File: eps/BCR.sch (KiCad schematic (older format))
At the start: 3 parts, among them U23 LT3652EMSE, U25 LT3652EMSE, U26 LT3652EMSE

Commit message: bcr
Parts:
- added J?: SA1A, symbol Connector:Conn_01x05_Male
- added J?: SA1B, symbol Connector:Conn_01x05_Male
- added J?: SA2A, symbol Connector:Conn_01x05_Male
- added J?: SA2B, symbol Connector:Conn_01x05_Male
- added J?: SA3A, symbol Connector:Conn_01x05_Male
- added J?: SA3B, symbol Connector:Conn_01x05_Male
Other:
- moved on the sheet: U23, U25, U26
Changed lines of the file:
@@
 L Battery_Management:LT3652EMSE U23
 U 1 1 61832F84
-P 5100 2850
-F 0 "U23" H 5100 3531 50  0000 C CNN
-F 1 "LT3652EMSE" H 5100 3440 50  0000 C CNN
-F 2 "Package_SO:MSOP-12-1EP_3x4mm_P0.65mm_EP1.65x2.85mm" H 5100 2250 50  0001 C CNN
-F 3 "https://www.analog.com/media/en/technical-documentation/data-sheets/3652fe.pdf" H 5700 2050 50  0001 C CNN
-	1    5100 2850
+P 4100 2100
+F 0 "U23" H 4100 2781 50  0000 C CNN
+F 1 "LT3652EMSE" H 4100 2690 50  0000 C CNN
+F 2 "Package_SO:MSOP-12-1EP_3x4mm_P0.65mm_EP1.65x2.85mm" H 4100 1500 50  0001 C CNN
+F 3 "https://www.analog.com/media/en/technical-documentation/data-sheets/3652fe.pdf" H 4700 1300 50  0001 C CNN
+	1    4100 2100
 	1    0    0    -1
 $EndComp
@@
 L Battery_Management:LT3652EMSE U25
 U 1 1 6183C8D2
-P 7150 2850
-F 0 "U25" H 7150 3531 50  0000 C CNN
-F 1 "LT3652EMSE" H 7150 3440 50  0000 C CNN
-F 2 "Package_SO:MSOP-12-1EP_3x4mm_P0.65mm_EP1.65x2.85mm" H 7150 2250 50  0001 C CNN
-F 3 "https://www.analog.com/media/en/technical-documentation/data-sheets/3652fe.pdf" H 7750 2050 50  0001 C CNN
-	1    7150 2850
+P 4150 4350
+F 0 "U25" H 4150 5031 50  0000 C CNN
+F 1 "LT3652EMSE" H 4150 4940 50  0000 C CNN
+F 2 "Package_SO:MSOP-12-1EP_3x4mm_P0.65mm_EP1.65x2.85mm" H 4150 3750 50  0001 C CNN
+F 3 "https://www.analog.com/media/en/technical-documentation/data-sheets/3652fe.pdf" H 4750 3550 50  0001 C CNN
+	1    4150 4350
 	1    0    0    -1
 $EndComp
@@
 L Battery_Management:LT3652EMSE U26
 U 1 1 6183D07C
-P 8800 2850
-F 0 "U26" H 8800 3531 50  0000 C CNN
-F 1 "LT3652EMSE" H 8800 3440 50  0000 C CNN
-F 2 "Package_SO:MSOP-12-1EP_3x4mm_P0.65mm_EP1.65x2.85mm" H 8800 2250 50  0001 C CNN
-F 3 "https://www.analog.com/media/en/technical-documentation/data-sheets/3652fe.pdf" H 9400 2050 50  0001 C CNN
-	1    8800 2850
+P 4200 6250
+F 0 "U26" H 4200 6931 50  0000 C CNN
+F 1 "LT3652EMSE" H 4200 6840 50  0000 C CNN
+F 2 "Package_SO:MSOP-12-1EP_3x4mm_P0.65mm_EP1.65x2.85mm" H 4200 5650 50  0001 C CNN
+F 3 "https://www.analog.com/media/en/technical-documentation/data-sheets/3652fe.pdf" H 4800 5450 50  0001 C CNN
+	1    4200 6250
 	1    0    0    -1
 $EndComp
+$Comp
+L Connector:Conn_01x05_Male J?
+U 1 1 6182DEA2
+P 2200 2100
+F 0 "J?" H 2308 2481 50  0000 C CNN
+F 1 "SA1A" H 2308 2390 50  0000 C CNN
+F 2 "" H 2200 2100 50  0001 C CNN
+F 3 "~" H 2200 2100 50  0001 C CNN
+	1    2200 2100
+	1    0    0    -1
+$EndComp
+$Comp
+L Connector:Conn_01x05_Male J?
+U 1 1 6182F03D
+P 2200 2850
+F 0 "J?" H 2308 3231 50  0000 C CNN
+F 1 "SA1B" H 2308 3140 50  0000 C CNN
+F 2 "" H 2200 2850 50  0001 C CNN
+F 3 "~" H 2200 2850 50  0001 C CNN
+	1    2200 2850
+	1    0    0    -1
+$EndComp
+$Comp
+L Connector:Conn_01x05_Male J?
+U 1 1 61831EC4
+P 2200 4050
+F 0 "J?" H 2308 4431 50  0000 C CNN
+F 1 "SA2A" H 2308 4340 50  0000 C CNN
+F 2 "" H 2200 4050 50  0001 C CNN
+F 3 "~" H 2200 4050 50  0001 C CNN
+	1    2200 4050
+	1    0    0    -1
+$EndComp
+$Comp
+L Connector:Conn_01x05_Male J?
+U 1 1 61831ECA
+P 2200 4800
+F 0 "J?" H 2308 5181 50  0000 C CNN
+F 1 "SA2B" H 2308 5090 50  0000 C CNN
+F 2 "" H 2200 4800 50  0001 C CNN
+F 3 "~" H 2200 4800 50  0001 C CNN
+	1    2200 4800
+	1    0    0    -1
+$EndComp
+$Comp
+L Connector:Conn_01x05_Male J?
+U 1 1 618337DD
+P 2200 5800
+F 0 "J?" H 2308 6181 50  0000 C CNN
+F 1 "SA3A" H 2308 6090 50  0000 C CNN
+F 2 "" H 2200 5800 50  0001 C CNN
+F 3 "~" H 2200 5800 50  0001 C CNN
+	1    2200 5800
+	1    0    0    -1
+$EndComp
+$Comp
+L Connector:Conn_01x05_Male J?
+U 1 1 618337E3
+P 2200 6550
+F 0 "J?" H 2308 6931 50  0000 C CNN
+F 1 "SA3B" H 2308 6840 50  0000 C CNN
+F 2 "" H 2200 6550 50  0001 C CNN
+F 3 "~" H 2200 6550 50  0001 C CNN
+	1    2200 6550
+	1    0    0    -1
+$EndComp

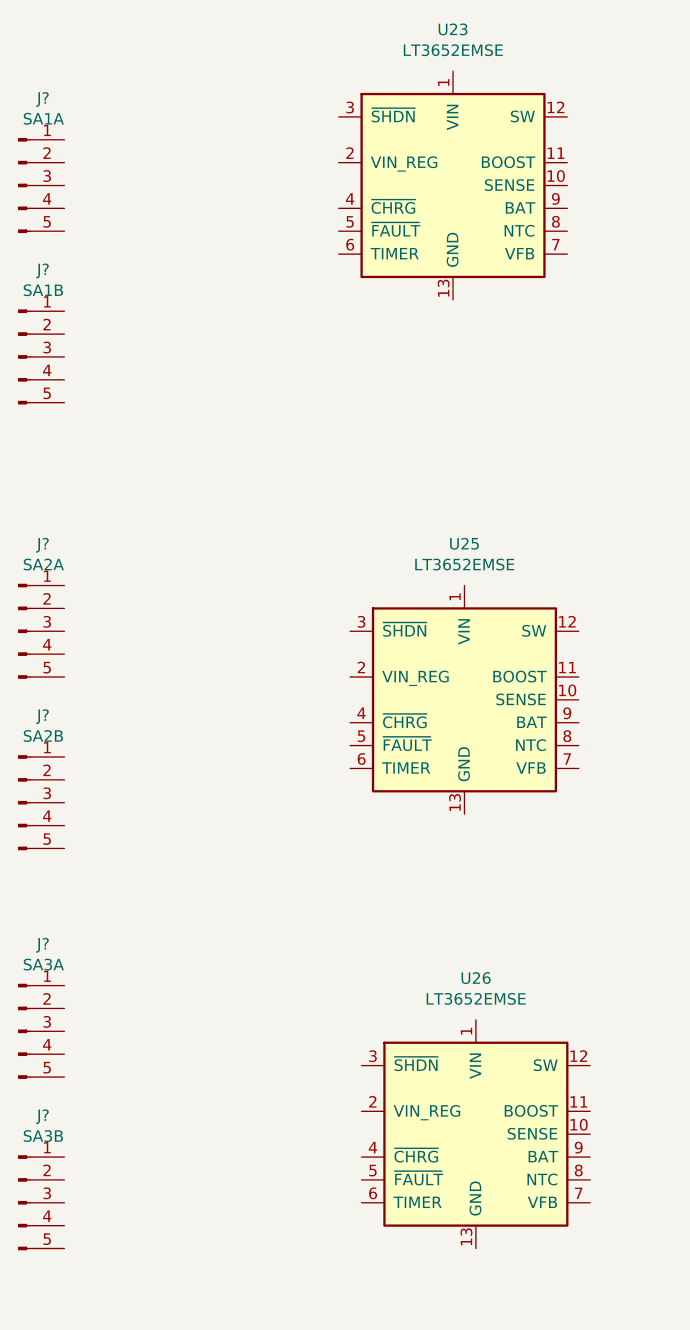
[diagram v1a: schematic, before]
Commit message: voltage dividers and move analog telem to new sheet
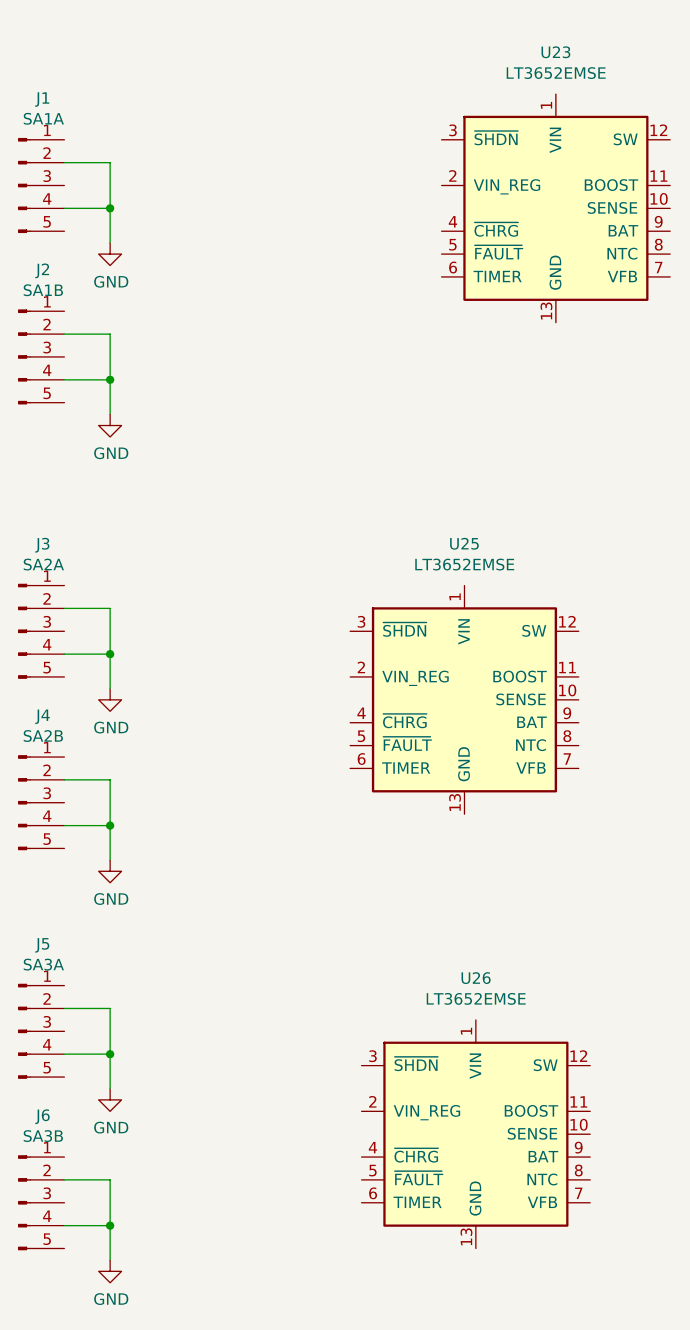
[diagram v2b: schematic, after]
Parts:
- gave numbers to parts that had none: 6
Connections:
- net GND: now reaches J1.2 (Pin_2)
- net GND: now also J1.4 (Pin_4), J2.2 (Pin_2), J2.4 (Pin_4), J3.2 (Pin_2), J3.4 (Pin_4), J4.2 (Pin_2), J4.4 (Pin_4), J5.2 (Pin_2), J5.4 (Pin_4), J6.2 (Pin_2), J6.4 (Pin_4)
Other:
- moved on the sheet: U23
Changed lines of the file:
@@
 $Descr A4 11693 8268
 encoding utf-8
-Sheet 7 7
+Sheet 7 8
 Title ""
 Date ""
@@
 L Battery_Management:LT3652EMSE U23
 U 1 1 61832F84
-P 4100 2100
-F 0 "U23" H 4100 2781 50  0000 C CNN
-F 1 "LT3652EMSE" H 4100 2690 50  0000 C CNN
-F 2 "Package_SO:MSOP-12-1EP_3x4mm_P0.65mm_EP1.65x2.85mm" H 4100 1500 50  0001 C CNN
-F 3 "https://www.analog.com/media/en/technical-documentation/data-sheets/3652fe.pdf" H 4700 1300 50  0001 C CNN
-	1    4100 2100
+P 4550 2200
+F 0 "U23" H 4550 2881 50  0000 C CNN
+F 1 "LT3652EMSE" H 4550 2790 50  0000 C CNN
+F 2 "Package_SO:MSOP-12-1EP_3x4mm_P0.65mm_EP1.65x2.85mm" H 4550 1600 50  0001 C CNN
+F 3 "https://www.analog.com/media/en/technical-documentation/data-sheets/3652fe.pdf" H 5150 1400 50  0001 C CNN
+	1    4550 2200
 	1    0    0    -1
 $EndComp
@@
 $EndComp
 $Comp
-L Connector:Conn_01x05_Male J?
+L Connector:Conn_01x05_Male J1
 U 1 1 6182DEA2
 P 2200 2100
-F 0 "J?" H 2308 2481 50  0000 C CNN
+F 0 "J1" H 2308 2481 50  0000 C CNN
 F 1 "SA1A" H 2308 2390 50  0000 C CNN
 F 2 "" H 2200 2100 50  0001 C CNN
@@
 $EndComp
 $Comp
-L Connector:Conn_01x05_Male J?
+L Connector:Conn_01x05_Male J2
 U 1 1 6182F03D
 P 2200 2850
-F 0 "J?" H 2308 3231 50  0000 C CNN
+F 0 "J2" H 2308 3231 50  0000 C CNN
 F 1 "SA1B" H 2308 3140 50  0000 C CNN
 F 2 "" H 2200 2850 50  0001 C CNN
@@
 $EndComp
 $Comp
-L Connector:Conn_01x05_Male J?
+L Connector:Conn_01x05_Male J3
 U 1 1 61831EC4
 P 2200 4050
-F 0 "J?" H 2308 4431 50  0000 C CNN
+F 0 "J3" H 2308 4431 50  0000 C CNN
 F 1 "SA2A" H 2308 4340 50  0000 C CNN
 F 2 "" H 2200 4050 50  0001 C CNN
@@
 $EndComp
 $Comp
-L Connector:Conn_01x05_Male J?
+L Connector:Conn_01x05_Male J4
 U 1 1 61831ECA
 P 2200 4800
-F 0 "J?" H 2308 5181 50  0000 C CNN
+F 0 "J4" H 2308 5181 50  0000 C CNN
 F 1 "SA2B" H 2308 5090 50  0000 C CNN
 F 2 "" H 2200 4800 50  0001 C CNN
@@
 $EndComp
 $Comp
-L Connector:Conn_01x05_Male J?
+L Connector:Conn_01x05_Male J5
 U 1 1 618337DD
 P 2200 5800
-F 0 "J?" H 2308 6181 50  0000 C CNN
+F 0 "J5" H 2308 6181 50  0000 C CNN
 F 1 "SA3A" H 2308 6090 50  0000 C CNN
 F 2 "" H 2200 5800 50  0001 C CNN
@@
 $EndComp
 $Comp
-L Connector:Conn_01x05_Male J?
+L Connector:Conn_01x05_Male J6
 U 1 1 618337E3
 P 2200 6550
-F 0 "J?" H 2308 6931 50  0000 C CNN
+F 0 "J6" H 2308 6931 50  0000 C CNN
 F 1 "SA3B" H 2308 6840 50  0000 C CNN
 F 2 "" H 2200 6550 50  0001 C CNN
@@
 	1    0    0    -1
 $EndComp
+Wire Wire Line
+	2400 2000 2600 2000
+Wire Wire Line
+	2600 2000 2600 2200
+Wire Wire Line
+	2400 2200 2600 2200
+Connection ~ 2600 2200
+Wire Wire Line
+	2600 2200 2600 2350
+Wire Wire Line
+	2400 2750 2600 2750
+Wire Wire Line
+	2600 2750 2600 2950
+Wire Wire Line
+	2400 2950 2600 2950
+Connection ~ 2600 2950
+Wire Wire Line
+	2600 2950 2600 3100
+Wire Wire Line
+	2400 3950 2600 3950
+Wire Wire Line
+	2600 3950 2600 4150
+Wire Wire Line
+	2400 4150 2600 4150
+Connection ~ 2600 4150
+Wire Wire Line
+	2600 4150 2600 4300
+Wire Wire Line
+	2400 4700 2600 4700
+Wire Wire Line
+	2600 4700 2600 4900
+Wire Wire Line
+	2400 4900 2600 4900
+Connection ~ 2600 4900
+Wire Wire Line
+	2600 4900 2600 5050
+Wire Wire Line
+	2400 5700 2600 5700
+Wire Wire Line
+	2600 5700 2600 5900
+Wire Wire Line
+	2400 5900 2600 5900
+Connection ~ 2600 5900
+Wire Wire Line
+	2600 5900 2600 6050
+Wire Wire Line
+	2400 6450 2600 6450
+Wire Wire Line
+	2600 6450 2600 6650
+Wire Wire Line
+	2400 6650 2600 6650
+Connection ~ 2600 6650
+Wire Wire Line
+	2600 6650 2600 6800
+$Comp
+L power:GND #PWR?
+U 1 1 61A89BE8
+P 2600 2350
+F 0 "#PWR?" H 2600 2100 50  0001 C CNN
+F 1 "GND" H 2605 2177 50  0000 C CNN
+F 2 "" H 2600 2350 50  0001 C CNN
+F 3 "" H 2600 2350 50  0001 C CNN
+	1    2600 2350
+	1    0    0    -1
+$EndComp
+$Comp
+L power:GND #PWR?
+U 1 1 61A8A4F9
+P 2600 3100
+F 0 "#PWR?" H 2600 2850 50  0001 C CNN
+F 1 "GND" H 2605 2927 50  0000 C CNN
+F 2 "" H 2600 3100 50  0001 C CNN
+F 3 "" H 2600 3100 50  0001 C CNN
+	1    2600 3100
+	1    0    0    -1
+$EndComp
+$Comp
+L power:GND #PWR?
+U 1 1 61A8A8F0
+P 2600 4300
+F 0 "#PWR?" H 2600 4050 50  0001 C CNN
+F 1 "GND" H 2605 4127 50  0000 C CNN
+F 2 "" H 2600 4300 50  0001 C CNN
+F 3 "" H 2600 4300 50  0001 C CNN
+	1    2600 4300
+	1    0    0    -1
+$EndComp
+$Comp
+L power:GND #PWR?
+U 1 1 61A8ABF9
+P 2600 5050
+F 0 "#PWR?" H 2600 4800 50  0001 C CNN
+F 1 "GND" H 2605 4877 50  0000 C CNN
+F 2 "" H 2600 5050 50  0001 C CNN
+F 3 "" H 2600 5050 50  0001 C CNN
+	1    2600 5050
+	1    0    0    -1
+$EndComp
+$Comp
+L power:GND #PWR?
+U 1 1 61A8AF32
+P 2600 6050
+F 0 "#PWR?" H 2600 5800 50  0001 C CNN
+F 1 "GND" H 2605 5877 50  0000 C CNN
+F 2 "" H 2600 6050 50  0001 C CNN
+F 3 "" H 2600 6050 50  0001 C CNN
+	1    2600 6050
+	1    0    0    -1
+$EndComp
+$Comp
+L power:GND #PWR?
+U 1 1 61A8B411
+P 2600 6800
+F 0 "#PWR?" H 2600 6550 50  0001 C CNN
+F 1 "GND" H 2605 6627 50  0000 C CNN
+F 2 "" H 2600 6800 50  0001 C CNN
+F 3 "" H 2600 6800 50  0001 C CNN
+	1    2600 6800
+	1    0    0    -1
+$EndComp

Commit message: bcr work
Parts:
- removed U23, U25, U26: LT3652EMSE, Package_SO:MSOP-12-1EP_3x4mm_P0.65mm_EP1.65x2.85mm, symbol Battery_Management:LT3652EMSE
- added R125, R126, R127, R128, R129, R130: 100K, symbol Device:R
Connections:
- net SA1AV: now reaches J1.1 (Pin_1)
- net TBCR1A: now reaches J1.3 (Pin_3)
- net TBCR1A: now also R125.2
- net BCR1/ADiode: now reaches J1.5 (Pin_5)
- net SA1BV: now reaches J2.1 (Pin_1)
- net TBCR1B: now reaches J2.3 (Pin_3)
- net TBCR1B: now also R126.2
- net BCR1/BDiode: now reaches J2.5 (Pin_5)
- net SA2AV: now reaches J3.1 (Pin_1)
- net TBCR2A: now reaches J3.3 (Pin_3)
- net TBCR2A: now also R127.2
- net BCR2/ADiode: now reaches J3.5 (Pin_5)
- net SA2BV: now reaches J4.1 (Pin_1)
- net TBCR2B: now reaches J4.3 (Pin_3)
- net TBCR2B: now also R128.2
- net BCR2/BDiode: now reaches J4.5 (Pin_5)
- net SA3AV: now reaches J5.1 (Pin_1)
- net TBCR3A: now reaches J5.3 (Pin_3)
- net TBCR3A: now also R129.2
- net BCR3/ADiode: now reaches J5.5 (Pin_5)
- net SA3BV: now reaches J6.1 (Pin_1)
- net TBCR3B: now reaches J6.3 (Pin_3)
- net TBCR3B: now also R130.2
- net BCR3/BDiode: now reaches J6.5 (Pin_5)
- new net VCC: R125.1, R126.1, R127.1, R128.1, R129.1, R130.1
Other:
- note added: "STAT pin indicates which of the panel connectors is feeding BCR.\n(outputs high when the connector is supplying charge)"
- note added: "pin 2 gnd should be connected to BCR power (could be connected to ground plane)\npin 4 gnd is common gnd for sensors and should be connected directly to ADC as an analog gnd"
- note added: "pin 3 is a PTC thermistor to ground"
- note added: "pin 5 is a photodiode cathode (anode connected to gnd)\n"
- moved on the sheet: J1, J3, J4, J5, J6

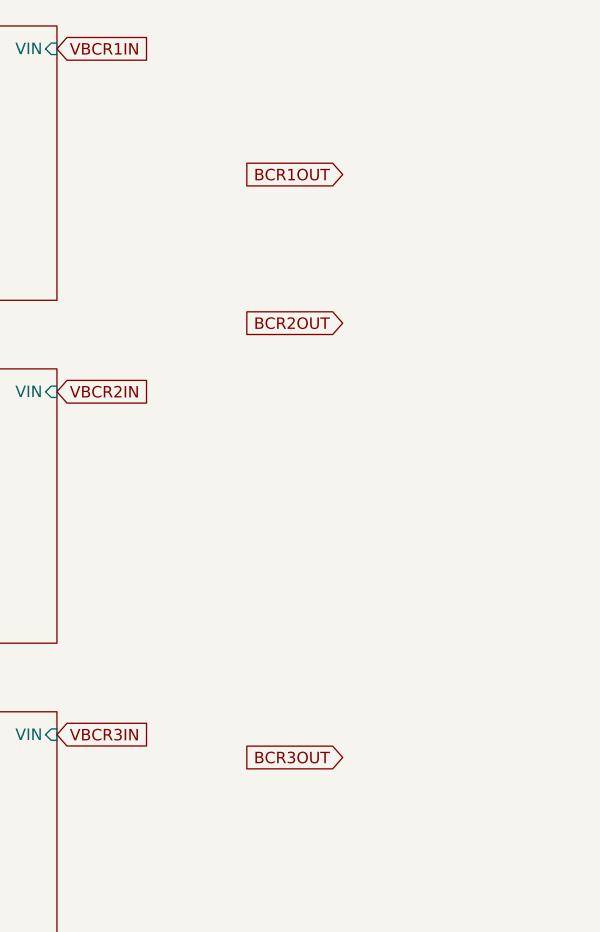
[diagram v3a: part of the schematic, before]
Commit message: start on adding LCLs to PDMs
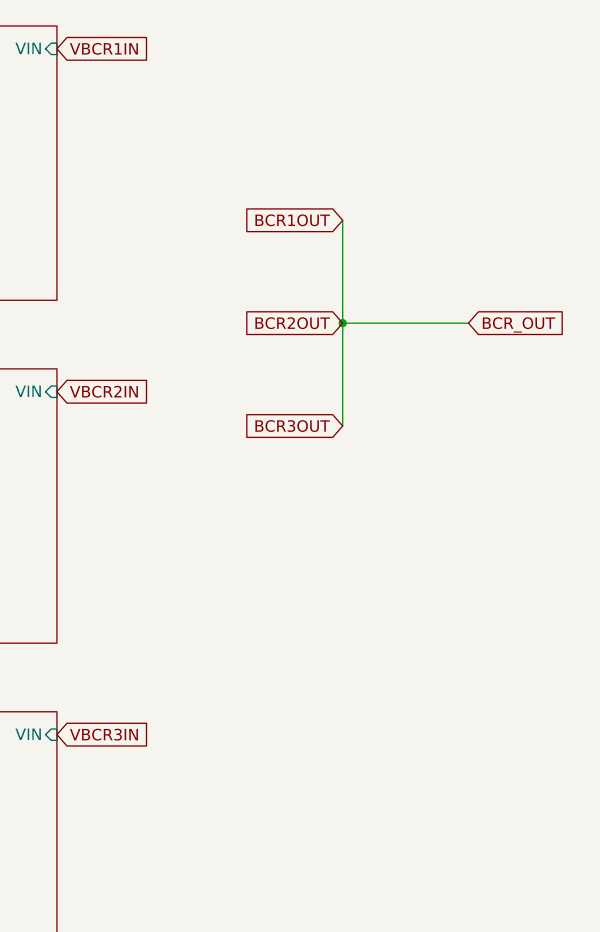
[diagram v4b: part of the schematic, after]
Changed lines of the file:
@@
 Text GLabel 3350 5700 0    50   Input ~ 0
 SDBCR3B
-Text GLabel 5450 2350 0    50   Input ~ 0
+Text GLabel 5450 2550 0    50   Input ~ 0
 BCR1OUT
 Text Notes 2700 1400 0    50   ~ 0
@@
 Text GLabel 5450 3000 0    50   Input ~ 0
 BCR2OUT
-Text GLabel 5450 4900 0    50   Input ~ 0
+Text GLabel 5450 3450 0    50   Input ~ 0
 BCR3OUT
 Text Notes 1250 5950 1    50   ~ 0
@@
 Text GLabel 4200 4800 2    50   Input ~ 0
 VBCR3IN
+Wire Wire Line
+	5450 2550 5450 3000
+Wire Wire Line
+	5450 3000 6000 3000
+Connection ~ 5450 3000
+Wire Wire Line
+	5450 3000 5450 3450
+Text GLabel 6000 3000 2    50   Input ~ 0
+BCR_OUT
 $EndSCHEMATC
